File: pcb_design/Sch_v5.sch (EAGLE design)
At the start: 32 parts

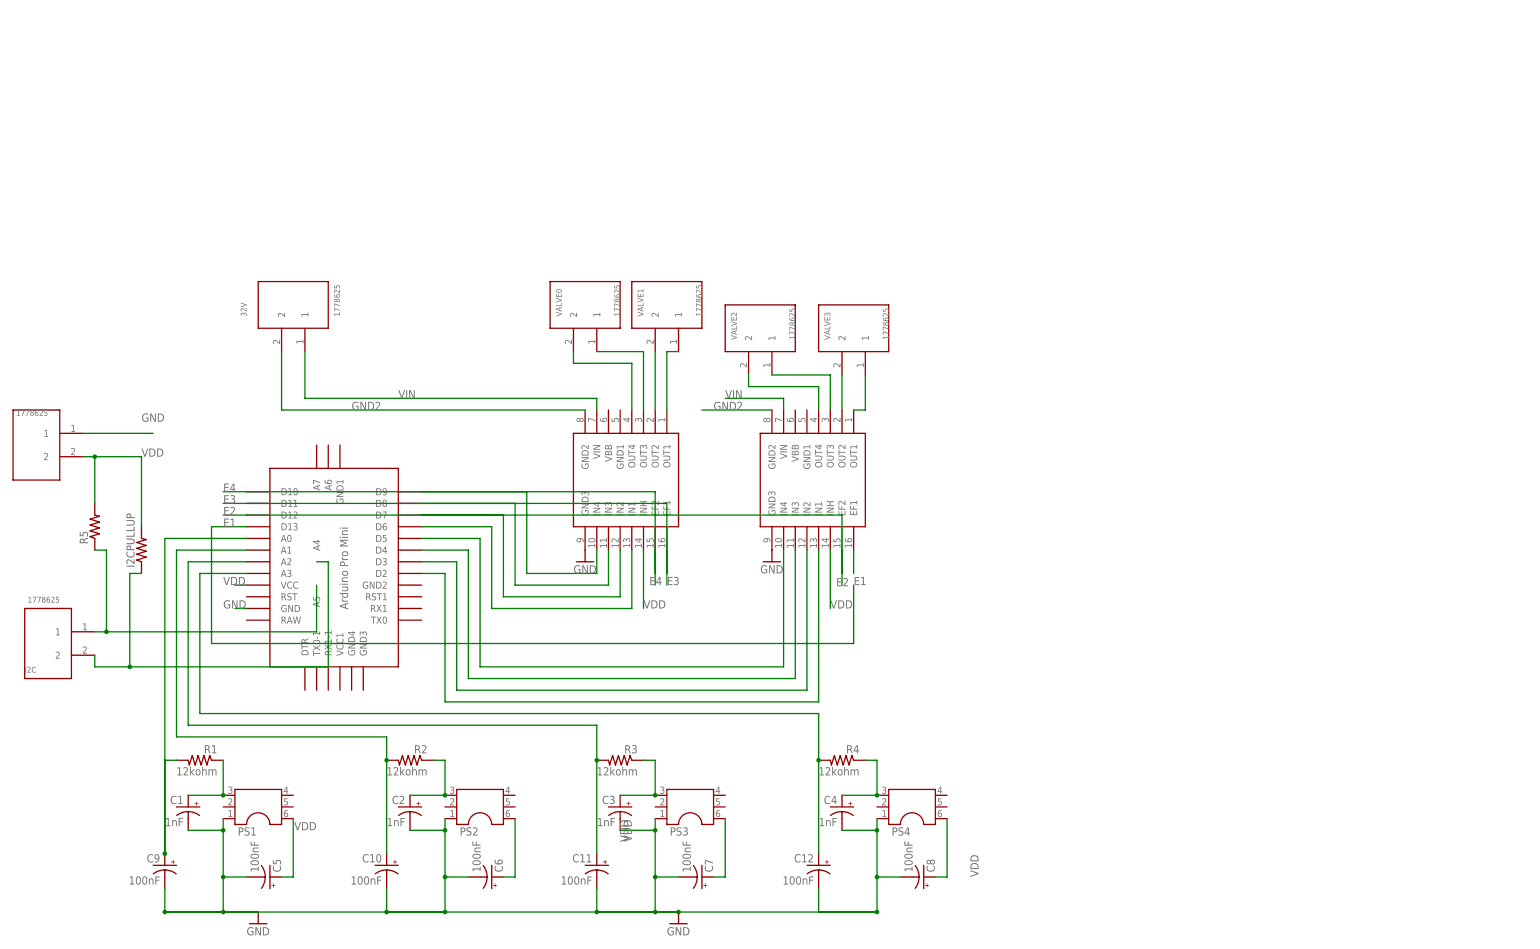
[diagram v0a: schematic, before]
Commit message: updated to v5. Cleaned up schematic a bit. Still need to fix I2C, flipped pins, etc.
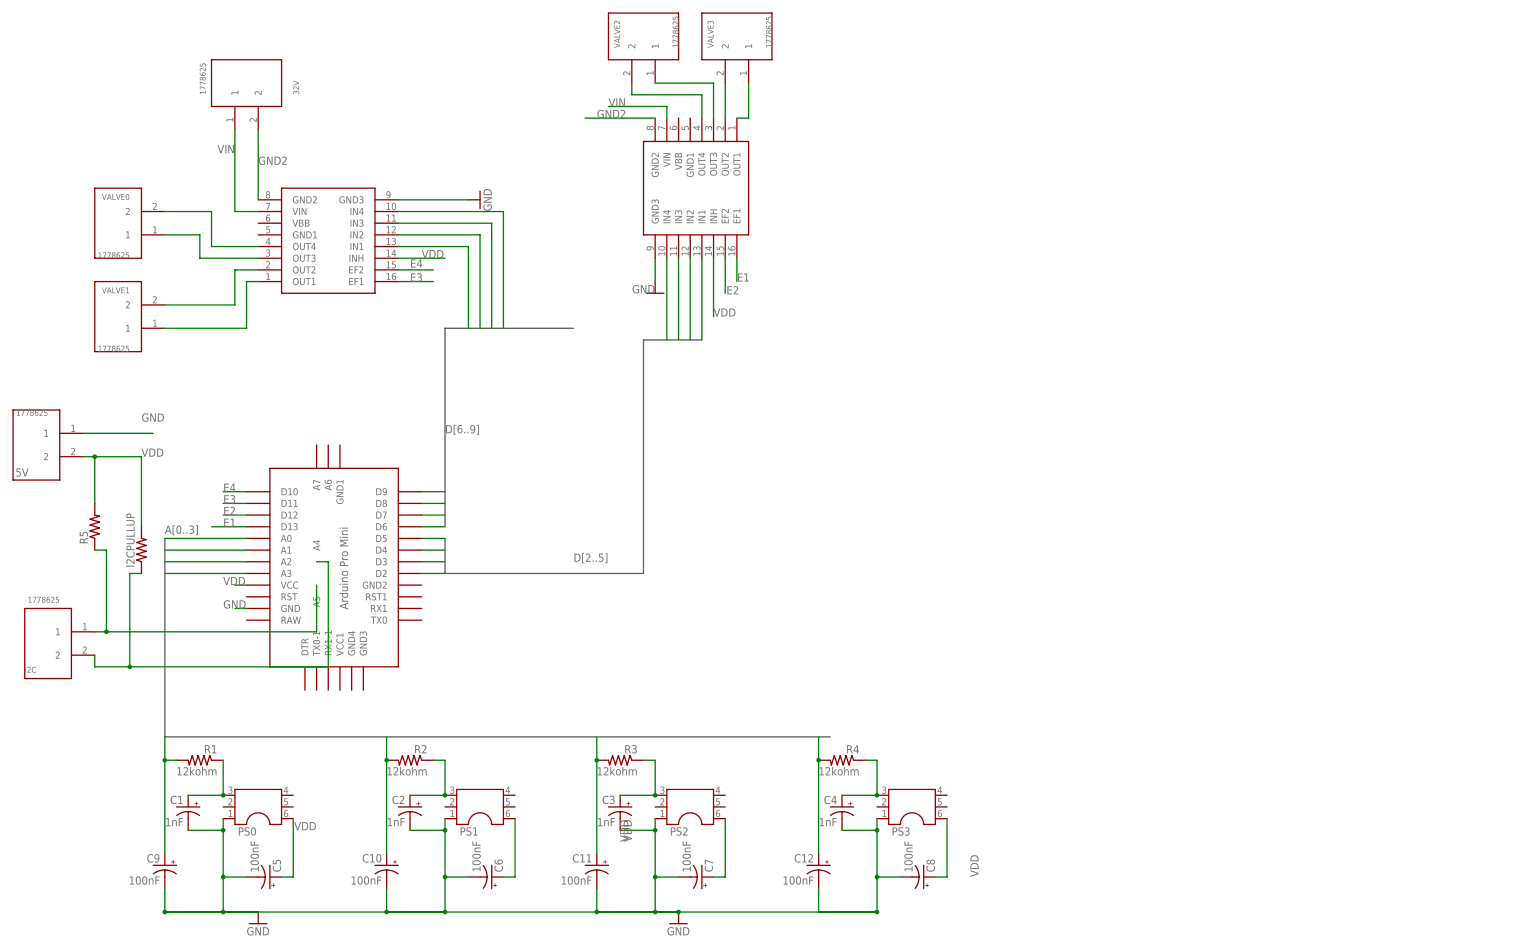
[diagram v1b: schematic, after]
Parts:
- removed PS4: (no value), RAD_2:ABPDRNN100PGAA5
- added PS0: (no value), RAD_2:ABPDRNN100PGAA5
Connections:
- net N$10 renamed A1
- net N$11 renamed A2
- net N$12 renamed A3
- net N$17 renamed D2
- net N$18 renamed D3
- net N$19 renamed D4
- net N$20 renamed D5
- net N$23 renamed D6
- net N$24 renamed D7
- net N$25 renamed D8
- net N$26 renamed D9
- net N$9 renamed A0
- net GND: now also PS0.1; no longer PS4.1
- net N$1: now also PS0.3; no longer PS1.3
- net N$2: now also PS1.3; no longer PS2.3
- net N$3: now also PS2.3; no longer PS3.3
- net N$4: now also PS3.3; no longer PS4.3
- net VDD: now also PS0.6; no longer PS4.6
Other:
- note added: "5V"
- moved on the sheet: 32V, PS1, PS2, PS3, VALVE0, VALVE1, VALVE2, VALVE3

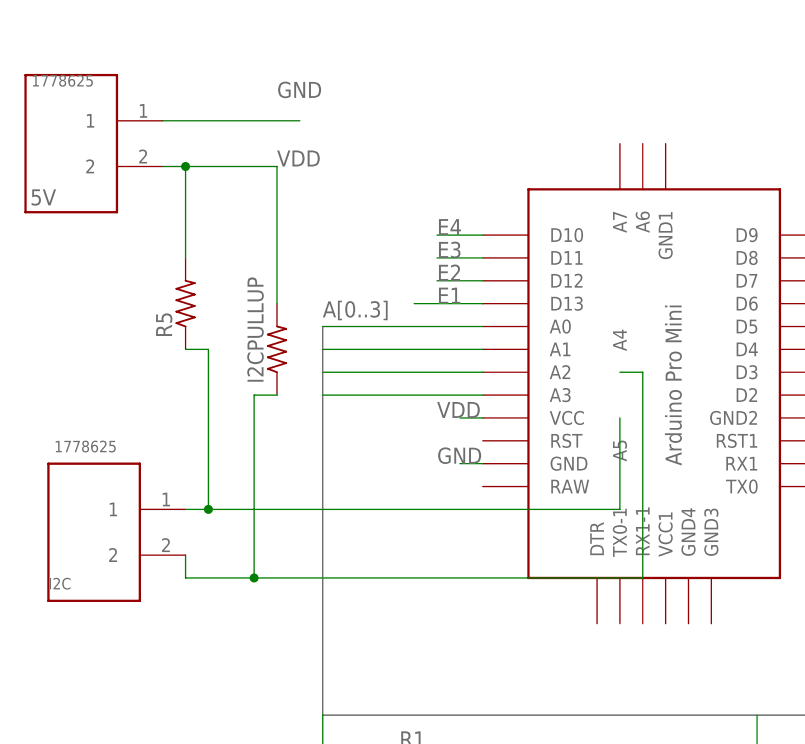
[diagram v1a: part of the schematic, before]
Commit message: Fixed I2C traces, changed power on arduino from VCC pin to Raw, updated silkscreen
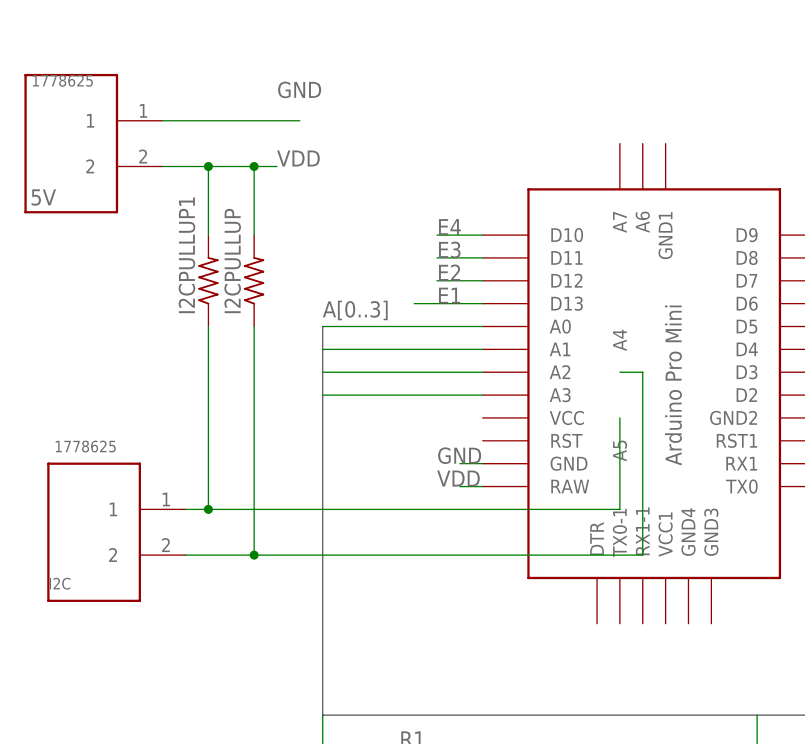
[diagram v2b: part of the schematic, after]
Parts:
- removed R5: (no value), rcl:R-US_0204/7
- added I2CPULLUP1: (no value), rcl:R-US_0204/7
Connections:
- new net N$9: I2C.2, I2CPULLUP.1, U$1.A4
- net N$21: now also I2CPULLUP1.1; no longer R5.1
- net VDD: now also I2CPULLUP1.2, U$1.RAW; no longer I2C.2, I2CPULLUP.1, R5.2, U$1.A4, U$1.VCC
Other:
- moved on the sheet: I2CPULLUP
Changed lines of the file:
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@@
 <part name="GND1" library="supply1" library_urn="urn:adsk.eagle:library:371" deviceset="GND" device=""/>
 <part name="GND2" library="supply1" library_urn="urn:adsk.eagle:library:371" deviceset="GND" device=""/>
-<part name="R5" library="rcl" library_urn="urn:adsk.eagle:library:334" deviceset="R-US_" device="0204/7" package3d_urn="urn:adsk.eagle:package:23498/2"/>
-<part name="I2CPULLUP" library="rcl" library_urn="urn:adsk.eagle:library:334" deviceset="R-US_" device="0204/7" package3d_urn="urn:adsk.eagle:package:23498/2"/>
 <part name="32V" library="1778625" deviceset="1778625" device=""/>
 <part name="VALVE0" library="1778625" deviceset="1778625" device=""/>
@@
 <part name="5V" library="1778625" deviceset="1778625" device=""/>
 <part name="I2C" library="1778625" deviceset="1778625" device=""/>
+<part name="I2CPULLUP" library="rcl" library_urn="urn:adsk.eagle:library:334" deviceset="R-US_" device="0204/7" package3d_urn="urn:adsk.eagle:package:23498/2"/>
+<part name="I2CPULLUP1" library="rcl" library_urn="urn:adsk.eagle:library:334" deviceset="R-US_" device="0204/7" package3d_urn="urn:adsk.eagle:package:23498/2"/>
 </parts>
 <sheets>
@@
 <attribute name="VALUE" x="88.9" y="142.24" size="1.778" layer="96" rot="MR0"/>
 </instance>
-<instance part="R5" gate="G$1" x="-33.02" y="91.44" smashed="yes" rot="R90">
-<attribute name="NAME" x="-34.5186" y="87.63" size="1.778" layer="95" rot="R90"/>
-<attribute name="VALUE" x="-29.718" y="87.63" size="1.778" layer="96" rot="R90"/>
-</instance>
-<instance part="I2CPULLUP" gate="G$1" x="-22.86" y="86.36" smashed="yes" rot="R90">
-<attribute name="NAME" x="-24.3586" y="82.55" size="1.778" layer="95" rot="R90"/>
-<attribute name="VALUE" x="-19.558" y="82.55" size="1.778" layer="96" rot="R90"/>
-</instance>
 <instance part="32V" gate="G$1" x="-7.62" y="182.88" smashed="yes" rot="MR90">
 <attribute name="NAME" x="10.16" y="185.42" size="1.27" layer="95" rot="MR90"/>
@@
 <attribute name="NAME" x="-45.72" y="60.96" size="1.27" layer="95" rot="R180"/>
 <attribute name="VALUE" x="-40.64" y="76.2" size="1.27" layer="96" rot="R180"/>
+</instance>
+<instance part="I2CPULLUP" gate="G$1" x="-25.4" y="93.98" smashed="yes" rot="R90">
+<attribute name="NAME" x="-26.8986" y="90.17" size="1.778" layer="95" rot="R90"/>
+<attribute name="VALUE" x="-22.098" y="90.17" size="1.778" layer="96" rot="R90"/>
+</instance>
+<instance part="I2CPULLUP1" gate="G$1" x="-30.48" y="93.98" smashed="yes" rot="R90">
+<attribute name="NAME" x="-31.9786" y="90.17" size="1.778" layer="95" rot="R90"/>
+<attribute name="VALUE" x="-27.178" y="90.17" size="1.778" layer="96" rot="R90"/>
 </instance>
 </instances>
@@
 </segment>
 <segment>
-<pinref part="U$1" gate="G$1" pin="A4"/>
-<wire x1="17.78" y1="83.82" x2="15.24" y2="83.82" width="0.1524" layer="91"/>
-<wire x1="-25.4" y1="60.96" x2="17.78" y2="60.96" width="0.1524" layer="91"/>
-<wire x1="17.78" y1="60.96" x2="17.78" y2="83.82" width="0.1524" layer="91"/>
-<pinref part="I2CPULLUP" gate="G$1" pin="1"/>
-<wire x1="-25.4" y1="60.96" x2="-25.4" y2="81.28" width="0.1524" layer="91"/>
-<wire x1="-25.4" y1="81.28" x2="-22.86" y2="81.28" width="0.1524" layer="91"/>
-<junction x="-25.4" y="60.96"/>
-<pinref part="I2C" gate="G$1" pin="2"/>
-<wire x1="-33.02" y1="63.5" x2="-33.02" y2="60.96" width="0.1524" layer="91"/>
-<wire x1="-33.02" y1="60.96" x2="-25.4" y2="60.96" width="0.1524" layer="91"/>
-</segment>
-<segment>
-<pinref part="U$1" gate="G$1" pin="VCC"/>
-<wire x1="0" y1="78.74" x2="-2.54" y2="78.74" width="0.1524" layer="91"/>
-<label x="-5.08" y="78.74" size="1.778" layer="95"/>
-</segment>
-<segment>
 <label x="-22.86" y="106.68" size="1.778" layer="95"/>
-<pinref part="R5" gate="G$1" pin="2"/>
-<wire x1="-33.02" y1="96.52" x2="-33.02" y2="106.68" width="0.1524" layer="91"/>
-<wire x1="-33.02" y1="106.68" x2="-22.86" y2="106.68" width="0.1524" layer="91"/>
+<wire x1="-30.48" y1="99.06" x2="-30.48" y2="106.68" width="0.1524" layer="91"/>
+<wire x1="-30.48" y1="106.68" x2="-25.4" y2="106.68" width="0.1524" layer="91"/>
+<pinref part="5V" gate="G$1" pin="2"/>
+<wire x1="-25.4" y1="106.68" x2="-22.86" y2="106.68" width="0.1524" layer="91"/>
+<wire x1="-35.56" y1="106.68" x2="-30.48" y2="106.68" width="0.1524" layer="91"/>
+<junction x="-30.48" y="106.68"/>
+<wire x1="-25.4" y1="99.06" x2="-25.4" y2="106.68" width="0.1524" layer="91"/>
+<junction x="-25.4" y="106.68"/>
 <pinref part="I2CPULLUP" gate="G$1" pin="2"/>
-<wire x1="-22.86" y1="91.44" x2="-22.86" y2="106.68" width="0.1524" layer="91"/>
-<pinref part="5V" gate="G$1" pin="2"/>
-<wire x1="-35.56" y1="106.68" x2="-33.02" y2="106.68" width="0.1524" layer="91"/>
-<junction x="-33.02" y="106.68"/>
+<pinref part="I2CPULLUP1" gate="G$1" pin="2"/>
+</segment>
+<segment>
+<pinref part="U$1" gate="G$1" pin="RAW"/>
+<wire x1="0" y1="71.12" x2="-2.54" y2="71.12" width="0.1524" layer="91"/>
+<label x="-5.08" y="71.12" size="1.778" layer="95"/>
 </segment>
 </net>
@@
 <wire x1="-30.48" y1="68.58" x2="15.24" y2="68.58" width="0.1524" layer="91"/>
 <wire x1="15.24" y1="68.58" x2="15.24" y2="78.74" width="0.1524" layer="91"/>
-<pinref part="R5" gate="G$1" pin="1"/>
-<wire x1="-30.48" y1="68.58" x2="-30.48" y2="86.36" width="0.1524" layer="91"/>
-<wire x1="-30.48" y1="86.36" x2="-33.02" y2="86.36" width="0.1524" layer="91"/>
+<wire x1="-30.48" y1="68.58" x2="-30.48" y2="88.9" width="0.1524" layer="91"/>
 <pinref part="I2C" gate="G$1" pin="1"/>
 <wire x1="-30.48" y1="68.58" x2="-33.02" y2="68.58" width="0.1524" layer="91"/>
 <junction x="-30.48" y="68.58"/>
+<pinref part="I2CPULLUP1" gate="G$1" pin="1"/>
 </segment>
 </net>
@@
 </segment>
 </net>
+<net name="N$9" class="0">
+<segment>
+<pinref part="I2C" gate="G$1" pin="2"/>
+<wire x1="-33.02" y1="63.5" x2="-25.4" y2="63.5" width="0.1524" layer="91"/>
+<wire x1="-25.4" y1="63.5" x2="17.78" y2="63.5" width="0.1524" layer="91"/>
+<wire x1="17.78" y1="63.5" x2="17.78" y2="83.82" width="0.1524" layer="91"/>
+<pinref part="U$1" gate="G$1" pin="A4"/>
+<wire x1="17.78" y1="83.82" x2="15.24" y2="83.82" width="0.1524" layer="91"/>
+<wire x1="-25.4" y1="88.9" x2="-25.4" y2="63.5" width="0.1524" layer="91"/>
+<junction x="-25.4" y="63.5"/>
+<pinref part="I2CPULLUP" gate="G$1" pin="1"/>
+</segment>
+</net>
 </nets>
 </sheet>
 </sheets>
-<errors>
-</errors>
 </schematic>
 </drawing>
